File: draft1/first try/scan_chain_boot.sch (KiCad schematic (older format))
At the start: 5 parts

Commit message: good enough scan_chain_boot
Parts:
- gave numbers to parts that had none: 4
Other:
- note added: "Do not populate R7 if U6 is present"
- note added: "Do not populate R8 if R7 is present"
- note added: "Populate to directly connect Teensy to HARD RESET on SCM. Should configure Teensy to do open-drain pulldown since this SCM pin cannot take 3.3V"
- note added: "Pullup to keep HARD_RESET high when teensy is not plugged in; Only needed when U6 is present"
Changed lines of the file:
@@
 $Descr A4 11693 8268
 encoding utf-8
-Sheet 3 4
+Sheet 2 4
 Title ""
 Date ""
@@
 P 2900 4550
 AR Path="/5F3DDAE9" Ref="IC?"  Part="1"
-AR Path="/5F3B0B28/5F3DDAE9" Ref="IC?"  Part="1"
-F 0 "IC?" H 3550 4815 50  0000 C CNN
+AR Path="/5F3B0B28/5F3DDAE9" Ref="U5"  Part="1"
+F 0 "U5" H 3550 4815 50  0000 C CNN
 F 1 "74AVC4TD245PW,118" H 3550 4724 50  0000 C CNN
 F 2 "SamacSys_Parts:SOP65P640X110-16N" H 4050 4650 50  0001 L CNN
@@
 P 4200 5250
 AR Path="/5F3DDAFD" Ref="#PWR?"  Part="1"
-AR Path="/5F3B0B28/5F3DDAFD" Ref="#PWR?"  Part="1"
-F 0 "#PWR?" H 4200 5000 50  0001 C CNN
+AR Path="/5F3B0B28/5F3DDAFD" Ref="#PWR0120"  Part="1"
+F 0 "#PWR0120" H 4200 5000 50  0001 C CNN
 F 1 "GND" H 4205 5077 50  0000 C CNN
 F 2 "" H 4200 5250 50  0001 C CNN
@@
 P 2900 5250
 AR Path="/5F3DDB03" Ref="#PWR?"  Part="1"
-AR Path="/5F3B0B28/5F3DDB03" Ref="#PWR?"  Part="1"
-F 0 "#PWR?" H 2900 5000 50  0001 C CNN
+AR Path="/5F3B0B28/5F3DDB03" Ref="#PWR0121"  Part="1"
+F 0 "#PWR0121" H 2900 5000 50  0001 C CNN
 F 1 "GND" H 2905 5077 50  0000 C CNN
 F 2 "" H 2900 5250 50  0001 C CNN
@@
 P 4200 5150
 AR Path="/5F3DDB09" Ref="#PWR?"  Part="1"
-AR Path="/5F3B0B28/5F3DDB09" Ref="#PWR?"  Part="1"
-F 0 "#PWR?" H 4200 4900 50  0001 C CNN
+AR Path="/5F3B0B28/5F3DDB09" Ref="#PWR0122"  Part="1"
+F 0 "#PWR0122" H 4200 4900 50  0001 C CNN
 F 1 "GND" V 4205 5022 50  0000 R CNN
 F 2 "" H 4200 5150 50  0001 C CNN
@@
 P 2900 5150
 AR Path="/5F3DDB0F" Ref="#PWR?"  Part="1"
-AR Path="/5F3B0B28/5F3DDB0F" Ref="#PWR?"  Part="1"
-F 0 "#PWR?" H 2900 4900 50  0001 C CNN
+AR Path="/5F3B0B28/5F3DDB0F" Ref="#PWR0123"  Part="1"
+F 0 "#PWR0123" H 2900 4900 50  0001 C CNN
 F 1 "GND" V 2905 5022 50  0000 R CNN
 F 2 "" H 2900 5150 50  0001 C CNN
@@
 P 4200 4650
 AR Path="/5F3DDB15" Ref="#PWR?"  Part="1"
-AR Path="/5F3B0B28/5F3DDB15" Ref="#PWR?"  Part="1"
-F 0 "#PWR?" H 4200 4400 50  0001 C CNN
+AR Path="/5F3B0B28/5F3DDB15" Ref="#PWR0124"  Part="1"
+F 0 "#PWR0124" H 4200 4400 50  0001 C CNN
 F 1 "GND" V 4205 4522 50  0000 R CNN
 F 2 "" H 4200 4650 50  0001 C CNN
@@
 P 6850 5200
 AR Path="/5F3DDB1B" Ref="#PWR?"  Part="1"
-AR Path="/5F3B0B28/5F3DDB1B" Ref="#PWR?"  Part="1"
-F 0 "#PWR?" H 6850 4950 50  0001 C CNN
+AR Path="/5F3B0B28/5F3DDB1B" Ref="#PWR0125"  Part="1"
+F 0 "#PWR0125" H 6850 4950 50  0001 C CNN
 F 1 "GND" H 6855 5027 50  0000 C CNN
 F 2 "" H 6850 5200 50  0001 C CNN
@@
 P 6850 5100
 AR Path="/5F3DDB21" Ref="#PWR?"  Part="1"
-AR Path="/5F3B0B28/5F3DDB21" Ref="#PWR?"  Part="1"
-F 0 "#PWR?" H 6850 4850 50  0001 C CNN
+AR Path="/5F3B0B28/5F3DDB21" Ref="#PWR0126"  Part="1"
+F 0 "#PWR0126" H 6850 4850 50  0001 C CNN
 F 1 "GND" V 6855 4972 50  0000 R CNN
 F 2 "" H 6850 5100 50  0001 C CNN
@@
 P 8150 5200
 AR Path="/5F3DDB27" Ref="#PWR?"  Part="1"
-AR Path="/5F3B0B28/5F3DDB27" Ref="#PWR?"  Part="1"
-F 0 "#PWR?" H 8150 4950 50  0001 C CNN
+AR Path="/5F3B0B28/5F3DDB27" Ref="#PWR0127"  Part="1"
+F 0 "#PWR0127" H 8150 4950 50  0001 C CNN
 F 1 "GND" H 8155 5027 50  0000 C CNN
 F 2 "" H 8150 5200 50  0001 C CNN
@@
 P 6850 4600
 AR Path="/5F3DDB2D" Ref="#PWR?"  Part="1"
-AR Path="/5F3B0B28/5F3DDB2D" Ref="#PWR?"  Part="1"
-F 0 "#PWR?" H 6850 4350 50  0001 C CNN
+AR Path="/5F3B0B28/5F3DDB2D" Ref="#PWR0128"  Part="1"
+F 0 "#PWR0128" H 6850 4350 50  0001 C CNN
 F 1 "GND" V 6855 4472 50  0000 R CNN
 F 2 "" H 6850 4600 50  0001 C CNN
@@
 P 8150 4600
 AR Path="/5F3DDB33" Ref="#PWR?"  Part="1"
-AR Path="/5F3B0B28/5F3DDB33" Ref="#PWR?"  Part="1"
-F 0 "#PWR?" H 8150 4350 50  0001 C CNN
+AR Path="/5F3B0B28/5F3DDB33" Ref="#PWR0129"  Part="1"
+F 0 "#PWR0129" H 8150 4350 50  0001 C CNN
 F 1 "GND" V 8155 4472 50  0000 R CNN
 F 2 "" H 8150 4600 50  0001 C CNN
@@
 P 8150 5100
 AR Path="/5F3DDB39" Ref="#PWR?"  Part="1"
-AR Path="/5F3B0B28/5F3DDB39" Ref="#PWR?"  Part="1"
-F 0 "#PWR?" H 8150 4850 50  0001 C CNN
+AR Path="/5F3B0B28/5F3DDB39" Ref="#PWR0130"  Part="1"
+F 0 "#PWR0130" H 8150 4850 50  0001 C CNN
 F 1 "GND" V 8155 4972 50  0000 R CNN
 F 2 "" H 8150 5100 50  0001 C CNN
@@
 P 2900 4550
 AR Path="/5F3DDB3F" Ref="#PWR?"  Part="1"
-AR Path="/5F3B0B28/5F3DDB3F" Ref="#PWR?"  Part="1"
-F 0 "#PWR?" H 2900 4400 50  0001 C CNN
+AR Path="/5F3B0B28/5F3DDB3F" Ref="#PWR0131"  Part="1"
+F 0 "#PWR0131" H 2900 4400 50  0001 C CNN
 F 1 "+VBAT" H 2915 4723 50  0000 C CNN
 F 2 "" H 2900 4550 50  0001 C CNN
@@
 P 2900 4650
 AR Path="/5F3DDB45" Ref="#PWR?"  Part="1"
-AR Path="/5F3B0B28/5F3DDB45" Ref="#PWR?"  Part="1"
-F 0 "#PWR?" H 2900 4500 50  0001 C CNN
+AR Path="/5F3B0B28/5F3DDB45" Ref="#PWR0132"  Part="1"
+F 0 "#PWR0132" H 2900 4500 50  0001 C CNN
 F 1 "+VBAT" V 2915 4778 50  0000 L CNN
 F 2 "" H 2900 4650 50  0001 C CNN
@@
 P 6850 4500
 AR Path="/5F3DDB4B" Ref="#PWR?"  Part="1"
-AR Path="/5F3B0B28/5F3DDB4B" Ref="#PWR?"  Part="1"
-F 0 "#PWR?" H 6850 4350 50  0001 C CNN
+AR Path="/5F3B0B28/5F3DDB4B" Ref="#PWR0133"  Part="1"
+F 0 "#PWR0133" H 6850 4350 50  0001 C CNN
 F 1 "+VBAT" H 6865 4673 50  0000 C CNN
 F 2 "" H 6850 4500 50  0001 C CNN
@@
 P 10050 2450
 AR Path="/5F3DDB6B" Ref="J?"  Part="1"
-AR Path="/5F3B0B28/5F3DDB6B" Ref="J?"  Part="1"
-F 0 "J?" V 10267 2396 50  0000 C CNN
+AR Path="/5F3B0B28/5F3DDB6B" Ref="P4"  Part="1"
+F 0 "P4" V 10267 2396 50  0000 C CNN
 F 1 "Conn_01x24" V 10176 2396 50  0000 C CNN
 F 2 "Connector_PinHeader_2.54mm:PinHeader_1x24_P2.54mm_Vertical" H 10050 2450 50  0001 C CNN
@@
 ASC_EXT_OVERRIDE
 Wire Wire Line
-	9850 2350 9600 2350
-Wire Wire Line
-	9850 2450 9600 2450
-Wire Wire Line
-	9850 2550 9600 2550
+	9850 2350 9000 2350
+Wire Wire Line
+	9850 2450 9000 2450
+Wire Wire Line
+	9850 2550 9000 2550
 Wire Wire Line
 	9850 2750 9600 2750
@@
 P 9600 2750
 AR Path="/5F3DDBB1" Ref="#PWR?"  Part="1"
-AR Path="/5F3B0B28/5F3DDBB1" Ref="#PWR?"  Part="1"
-F 0 "#PWR?" H 9600 2500 50  0001 C CNN
+AR Path="/5F3B0B28/5F3DDBB1" Ref="#PWR0134"  Part="1"
+F 0 "#PWR0134" H 9600 2500 50  0001 C CNN
 F 1 "GND" V 9605 2622 50  0000 R CNN
 F 2 "" H 9600 2750 50  0001 C CNN
@@
 	0    1    1    0
 $EndComp
-Text HLabel 9600 2550 0    50   BiDi ~ 0
+Text HLabel 9000 2550 0    50   BiDi ~ 0
 3WB_DATA
-Text HLabel 9600 2450 0    50   BiDi ~ 0
+Text HLabel 9000 2450 0    50   BiDi ~ 0
 3WB_ENB
-Text HLabel 9600 2350 0    50   BiDi ~ 0
+Text HLabel 9000 2350 0    50   BiDi ~ 0
 3WB_CLK
 $Comp
@@
 P 4050 3250
 AR Path="/5F3DDBBA" Ref="R?"  Part="1"
-AR Path="/5F3B0B28/5F3DDBBA" Ref="R?"  Part="1"
-F 0 "R?" V 3845 3250 50  0000 C CNN
+AR Path="/5F3B0B28/5F3DDBBA" Ref="R7"  Part="1"
+F 0 "R7" V 3845 3250 50  0000 C CNN
 F 1 "NP" V 3936 3250 50  0000 C CNN
 F 2 "Resistor_SMD:R_0603_1608Metric" V 4090 3240 50  0001 C CNN
@@
 P 5000 2150
 AR Path="/5F3DDBC0" Ref="R?"  Part="1"
-AR Path="/5F3B0B28/5F3DDBC0" Ref="R?"  Part="1"
-F 0 "R?" V 4795 2150 50  0000 C CNN
+AR Path="/5F3B0B28/5F3DDBC0" Ref="R8"  Part="1"
+F 0 "R8" V 4795 2150 50  0000 C CNN
 F 1 "100k" V 4886 2150 50  0000 C CNN
 F 2 "Resistor_SMD:R_0603_1608Metric" V 5040 2140 50  0001 C CNN
@@
 P 4600 4550
 AR Path="/5F3DDBC6" Ref="#PWR?"  Part="1"
-AR Path="/5F3B0B28/5F3DDBC6" Ref="#PWR?"  Part="1"
-F 0 "#PWR?" H 4600 4400 50  0001 C CNN
+AR Path="/5F3B0B28/5F3DDBC6" Ref="#PWR0135"  Part="1"
+F 0 "#PWR0135" H 4600 4400 50  0001 C CNN
 F 1 "+UART33" H 4615 4723 50  0000 C CNN
 F 2 "" H 4600 4550 50  0001 C CNN
@@
 P 8550 4500
 AR Path="/5F3DDBCC" Ref="#PWR?"  Part="1"
-AR Path="/5F3B0B28/5F3DDBCC" Ref="#PWR?"  Part="1"
-F 0 "#PWR?" H 8550 4350 50  0001 C CNN
+AR Path="/5F3B0B28/5F3DDBCC" Ref="#PWR0136"  Part="1"
+F 0 "#PWR0136" H 8550 4350 50  0001 C CNN
 F 1 "+UART33" H 8565 4673 50  0000 C CNN
 F 2 "" H 8550 4500 50  0001 C CNN
@@
 P 4500 2150
 AR Path="/5F3DDBD9" Ref="#PWR?"  Part="1"
-AR Path="/5F3B0B28/5F3DDBD9" Ref="#PWR?"  Part="1"
-F 0 "#PWR?" H 4500 2000 50  0001 C CNN
+AR Path="/5F3B0B28/5F3DDBD9" Ref="#PWR0137"  Part="1"
+F 0 "#PWR0137" H 4500 2000 50  0001 C CNN
 F 1 "+UART33" H 4515 2323 50  0000 C CNN
 F 2 "" H 4500 2150 50  0001 C CNN
@@
 	1    0    0    -1
 $EndComp
+Text Notes 2550 2400 0    50   ~ 0
+Pullup to keep HARD_RESET high when teensy is not plugged in; Only needed when U6 is present
+Text Notes 2500 2650 0    50   ~ 0
+Do not populate R8 if R7 is present
+Text Notes 1450 3450 0    50   ~ 0
+Populate to directly connect Teensy to HARD RESET on SCM. Should configure Teensy to do open-drain pulldown since this SCM pin cannot take 3.3V
+Text Notes 2500 3750 0    50   ~ 0
+Do not populate R7 if U6 is present
+Text Label 9600 2350 2    50   ~ 0
+3WB_CLK
+Text Label 9600 2450 2    50   ~ 0
+3WB_ENB
+Text Label 9600 2550 2    50   ~ 0
+3WB_DATA
 $EndSCHEMATC

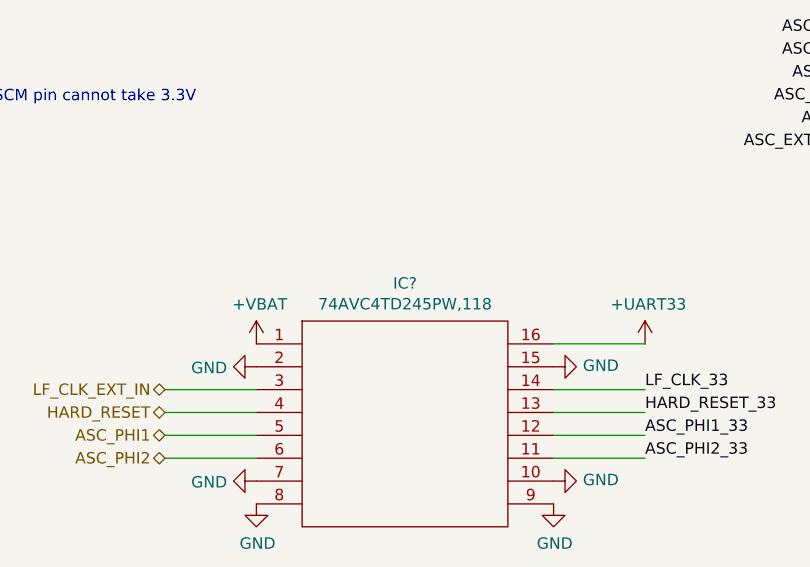
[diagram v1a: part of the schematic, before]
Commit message: UART good enough
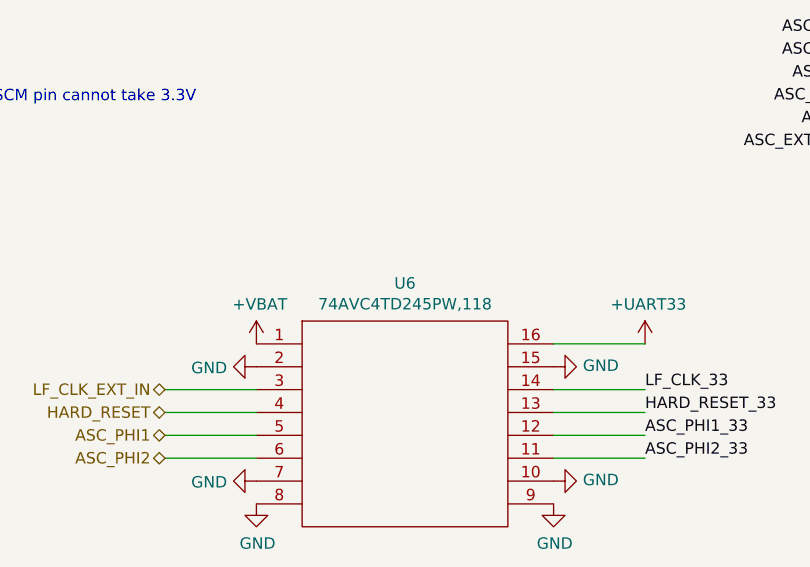
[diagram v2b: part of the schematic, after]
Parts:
- gave numbers to parts that had none: 1
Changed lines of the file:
@@
 P 6850 4500
 AR Path="/5F3DDAF7" Ref="IC?"  Part="1"
-AR Path="/5F3B0B28/5F3DDAF7" Ref="IC?"  Part="1"
-F 0 "IC?" H 7500 4765 50  0000 C CNN
+AR Path="/5F3B0B28/5F3DDAF7" Ref="U6"  Part="1"
+F 0 "U6" H 7500 4765 50  0000 C CNN
 F 1 "74AVC4TD245PW,118" H 7500 4674 50  0000 C CNN
 F 2 "SamacSys_Parts:SOP65P640X110-16N" H 8000 4600 50  0001 L CNN
